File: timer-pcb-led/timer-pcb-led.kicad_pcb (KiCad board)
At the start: 4 copper layers, 74.5 x 54 mm, 15 parts, among them J1 JST_03

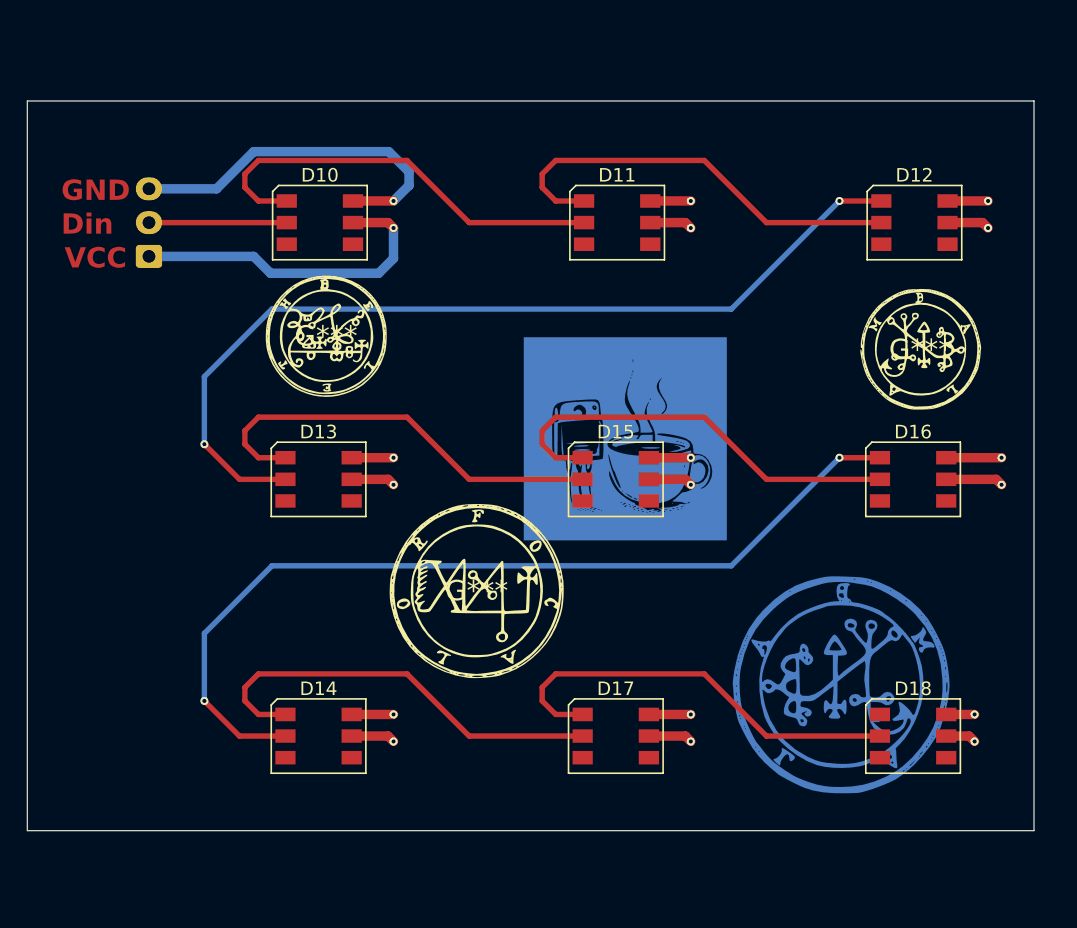
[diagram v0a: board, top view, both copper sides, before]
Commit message: rework des PCB stepper et led. création du PCB chargeur
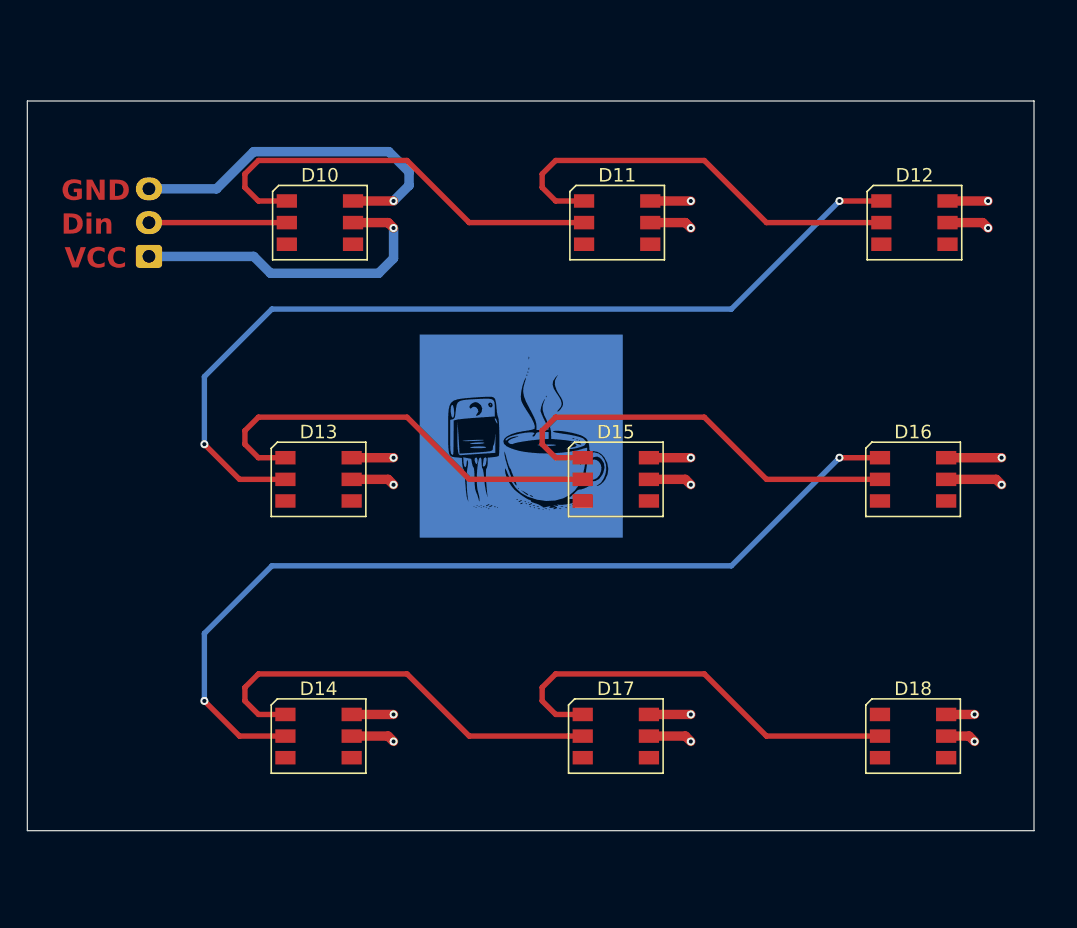
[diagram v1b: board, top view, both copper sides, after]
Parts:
- removed the G*** at (73.1, 136.4)
- removed the G*** at (84.2, 155.2)
- removed the G*** at (117.1, 137.4)
- removed the G*** at (111.2, 162.2)
- moved G*** 7.70 mm to (87.5, 143.8)

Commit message: suppression du dossier chargeur. integration de la partie chargeur usb-c sur le PCB stepper
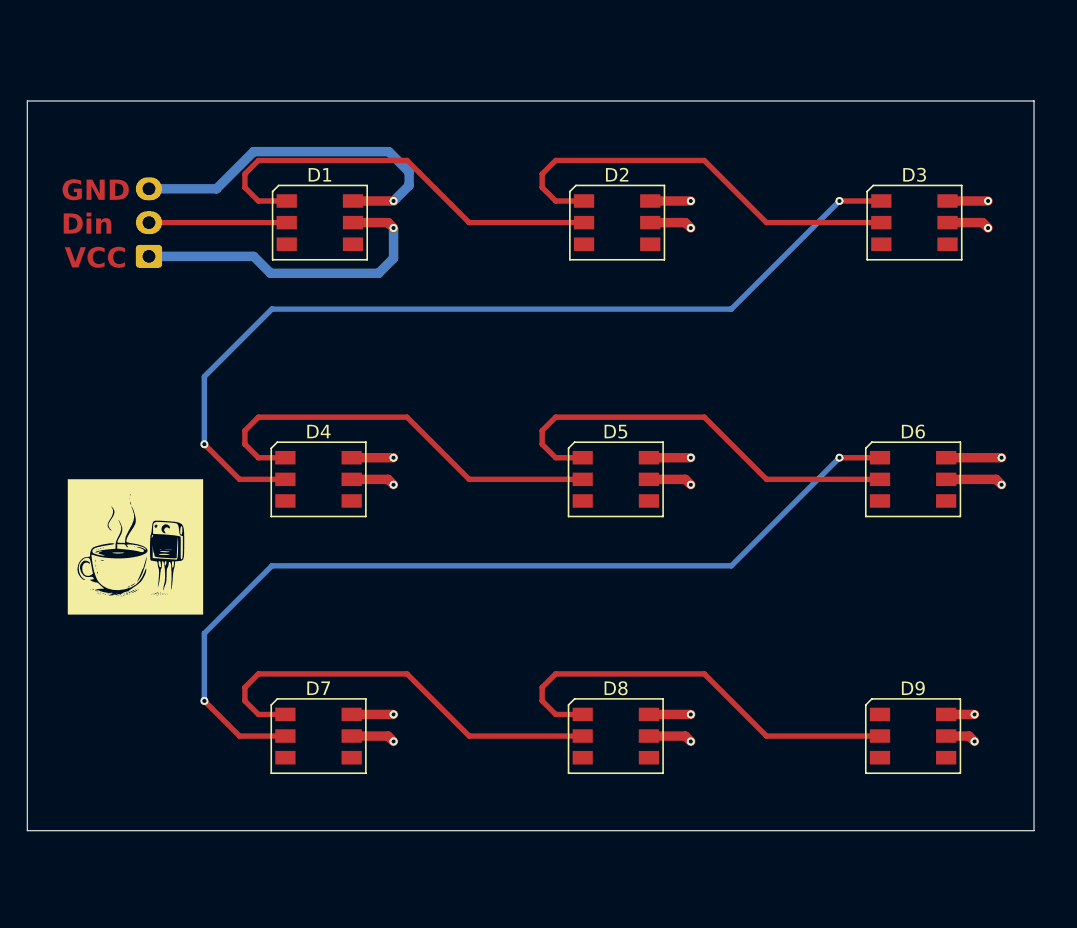
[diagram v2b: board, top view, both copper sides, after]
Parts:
- removed the G*** at (87.5, 143.8)
- added G***: LOGO, image.preety:logo_electrocafe_10x10, F.Cu at (59.0, 152.0)
- renumbered D10 to D1, D11 to D2, D12 to D3, D13 to D4, D15 to D5, D16 to D6, D14 to D7, D17 to D8, D18 to D9

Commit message: reroutage des liaisons pour avoir un circuit imprimé plus propre.
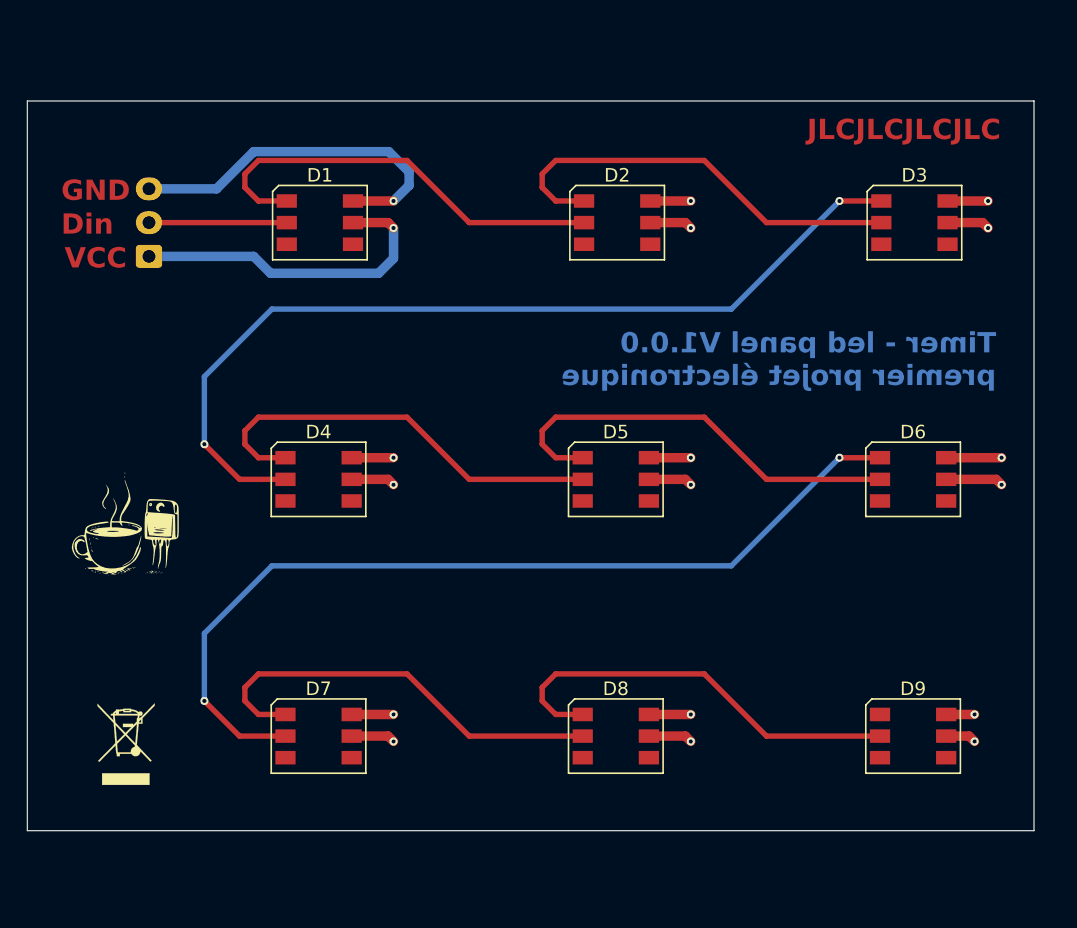
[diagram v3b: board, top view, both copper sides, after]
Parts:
- added REF**: WEEE-Logo_4.2x6mm_SilkScreen, Symbol:WEEE-Logo_4.2x6mm_SilkScreen, F.Cu at (58.3, 166.6)
- moved G*** 1.65 mm to (58.6, 150.4)
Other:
- board text added: "JLCJLCJLCJLC"
- board text added: "Timer - led panel V1.0.0 premier projet électronique"

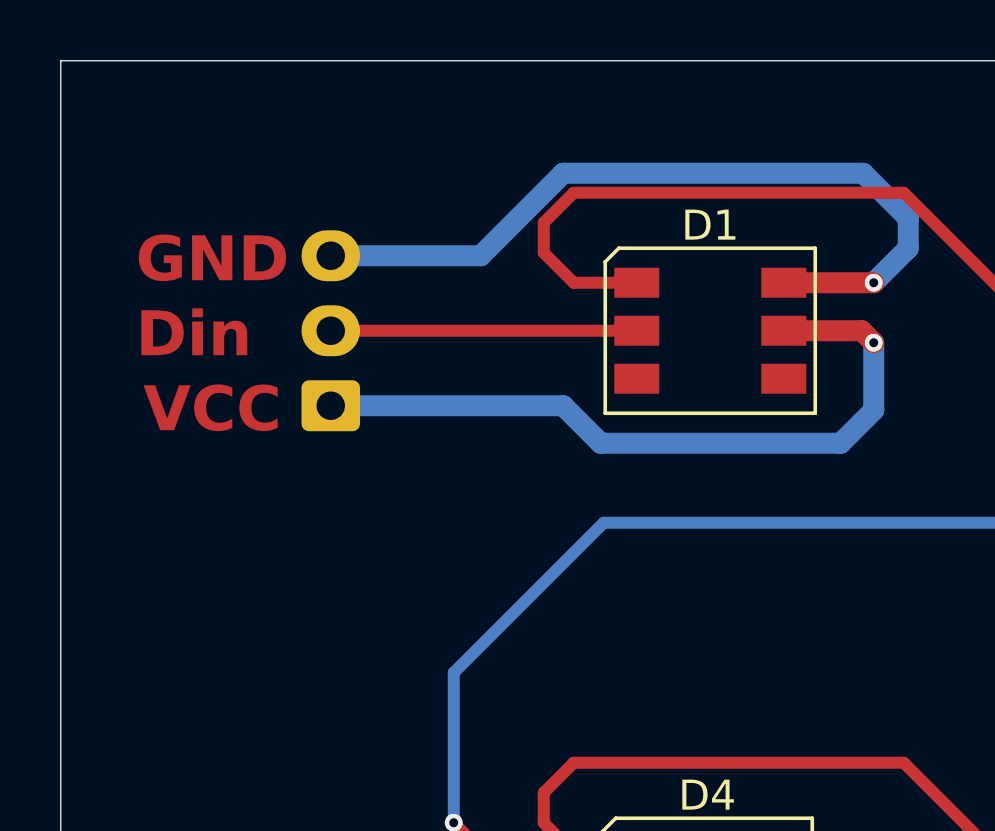
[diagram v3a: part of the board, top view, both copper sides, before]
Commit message: ajout de text indicatif couche silkscreen sur les différents composants du PCB. ajout de test points sur 5V, GND, GPIO37 pour debugger et pin 15 (3.3V). connecteurs repositionés franc bord.
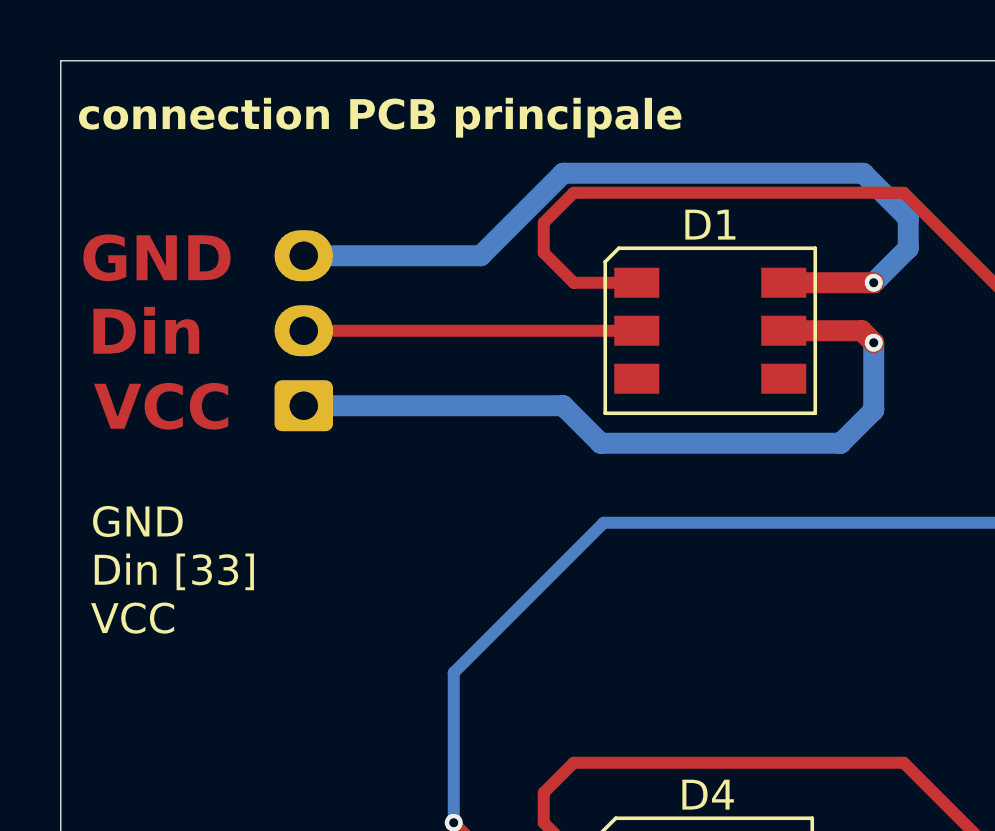
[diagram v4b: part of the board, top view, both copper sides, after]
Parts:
- moved J1 0.90 mm to (59.1, 130.5)
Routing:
- net +5V: track 50.4 -> 51.3 mm
- net GPIO33: track 10.2 -> 11.1 mm
- net GND: track 51.2 -> 52.1 mm
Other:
- board text added: "GND Din [33] VCC"
- board text added: "connection PCB principale"
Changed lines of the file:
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@@
 	(footprint "Connector_JST:JST_XH_S3B-XH-A-1_1x03_P2.50mm_Horizontal"
 		(layer "B.Cu")
-		(at 60 130.5 90)
+		(at 59.1 130.5 90)
 		(descr "JST XH series connector, S3B-XH-A-1 (http://www.jst-mfg.com/product/pdf/eng/eXH.pdf), generated with kicad-footprint-generator")
 		(tags "connector JST XH horizontal")
@@
 	)
 	(gr_text "GND"
-		(at 53.5 126.5 0)
+		(at 51.65 126.5 0)
 		(layer "F.Cu")
 		(effects
@@
 	)
 	(gr_text "Din"
-		(at 53.5 129 0)
+		(at 51.9 128.95 0)
 		(layer "F.Cu")
 		(effects
@@
 	)
 	(gr_text "VCC"
-		(at 53.75 131.5 0)
+		(at 52.1 131.45 0)
 		(layer "F.Cu")
 		(effects
@@
 		)
 	)
+	(gr_text "connection PCB principale"
+		(at 51.55 121.4 0)
+		(layer "F.SilkS")
+		(effects
+			(font
+				(size 1 1)
+				(thickness 0.25)
+				(bold yes)
+			)
+			(justify left bottom)
+		)
+	)
+	(gr_text "GND\nDin [33]\nVCC"
+		(at 52 138.2 0)
+		(layer "F.SilkS")
+		(effects
+			(font
+				(size 1 1)
+				(thickness 0.125)
+			)
+			(justify left bottom)
+		)
+	)
 	(segment
 		(start 97 145.4)
@@
 	)
 	(segment
-		(start 65 125.5)
-		(end 60 125.5)
+		(start 67.75 122.75)
+		(end 65 125.5)
+		(width 0.7)
+		(layer "B.Cu")
+		(net 1)
+	)
+	(segment
+		(start 79.25 125.25)
+		(end 79.25 124.25)
+		(width 0.7)
+		(layer "B.Cu")
+		(net 1)
+	)
+	(segment
+		(start 77.75 122.75)
+		(end 67.75 122.75)
 		(width 0.7)
 		(layer "B.Cu")
@@
 	)
 	(segment
-		(start 67.75 122.75)
-		(end 65 125.5)
-		(width 0.7)
-		(layer "B.Cu")
-		(net 1)
-	)
-	(segment
-		(start 77.75 122.75)
-		(end 67.75 122.75)
-		(width 0.7)
-		(layer "B.Cu")
-		(net 1)
-	)
-	(segment
-		(start 79.25 125.25)
-		(end 79.25 124.25)
+		(start 65 125.5)
+		(end 59.1 125.5)
 		(width 0.7)
 		(layer "B.Cu")
@@
 	(segment
 		(start 70.2 128)
-		(end 60 128)
+		(end 59.1 128)
 		(width 0.4)
 		(layer "F.Cu")
@@
 	)
 	(segment
+		(start 78.1 128.4)
+		(end 78.1 130.65)
+		(width 0.7)
+		(layer "B.Cu")
+		(net 9)
+	)
+	(segment
+		(start 77 131.75)
+		(end 69 131.75)
+		(width 0.7)
+		(layer "B.Cu")
+		(net 9)
+	)
+	(segment
+		(start 67.75 130.5)
+		(end 59.1 130.5)
+		(width 0.7)
+		(layer "B.Cu")
+		(net 9)
+	)
+	(segment
+		(start 78.1 130.65)
+		(end 77 131.75)
+		(width 0.7)
+		(layer "B.Cu")
+		(net 9)
+	)
+	(segment
 		(start 69 131.75)
 		(end 67.75 130.5)
 		(width 0.7)
 		(layer "B.Cu")
-		(net 9)
-	)
-	(segment
-		(start 77 131.75)
-		(end 69 131.75)
-		(width 0.7)
-		(layer "B.Cu")
-		(net 9)
-	)
-	(segment
-		(start 78.1 128.4)
-		(end 78.1 130.65)
-		(width 0.7)
-		(layer "B.Cu")
-		(net 9)
-	)
-	(segment
-		(start 78.1 130.65)
-		(end 77 131.75)
-		(width 0.7)
-		(layer "B.Cu")
-		(net 9)
-	)
-	(segment
-		(start 67.75 130.5)
-		(end 60 130.5)
-		(width 0.7)
-		(layer "B.Cu")

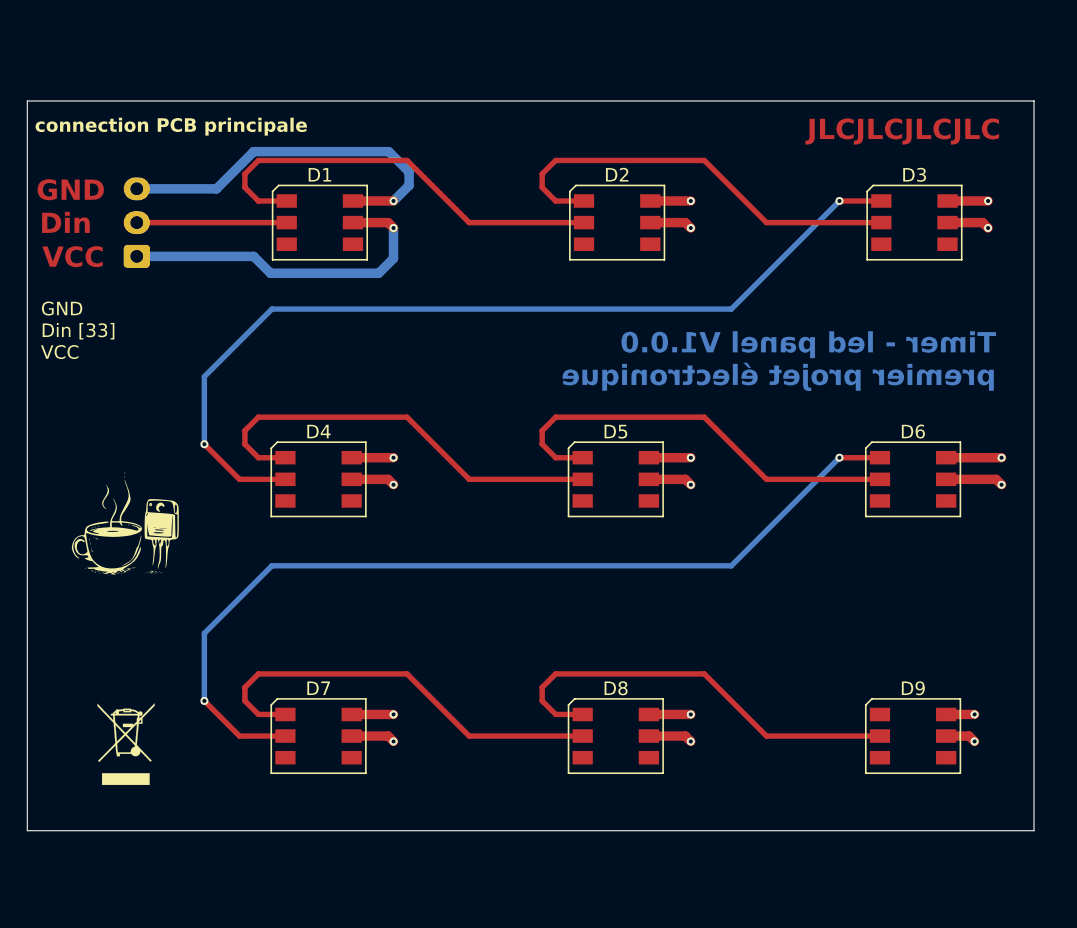
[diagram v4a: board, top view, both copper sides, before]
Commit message: mise à jour fichier blender pour impression 3D. Reste a mettre la bonne épaisseur pour le socle de la shell et percer les trous pour interrupteurs switch et on-off. déterminer ou placer entrées pour recharge et update code. comment fixer module recharge.
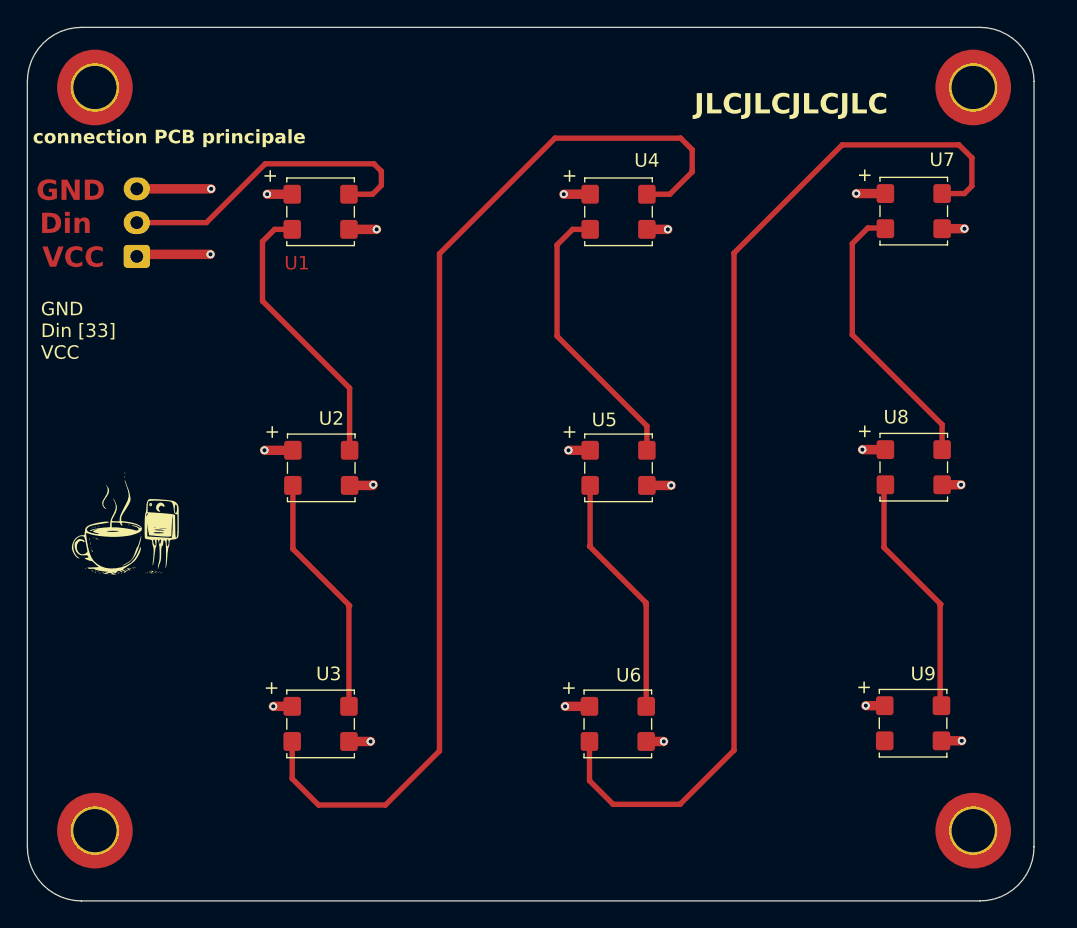
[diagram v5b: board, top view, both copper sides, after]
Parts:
- removed D1, D2, D3, D4, D5, D6, D7, D8, D9: WS2812, LED_SMD:LED_WS2812_PLCC6_5.0x5.0mm_P1.6mm
- removed REF**: WEEE-Logo_4.2x6mm_SilkScreen, Symbol:WEEE-Logo_4.2x6mm_SilkScreen
- added H1: MountingHole, MountingHole:MountingHole_3.2mm_M3_DIN965_Pad_TopOnly, F.Cu at (121.0, 118.0)
- added H2: MountingHole, MountingHole:MountingHole_3.2mm_M3_DIN965_Pad_TopOnly, F.Cu at (56.0, 118.0)
- added H3: MountingHole, MountingHole:MountingHole_3.2mm_M3_DIN965_Pad_TopOnly, F.Cu at (121.0, 173.0)
- added H4: MountingHole, MountingHole:MountingHole_3.2mm_M3_DIN965_Pad_TopOnly, F.Cu at (56.0, 173.0)
- added U1: , 1_My_Custom_Library:WS2812B-Xinlight-5050RGBC, F.Cu at (70.2, 124.7)
- added U2: ~, 1_My_Custom_Library:WS2812B-Xinlight-5050RGBC, F.Cu at (70.2, 143.7)
- added U3: ~, 1_My_Custom_Library:WS2812B-Xinlight-5050RGBC, F.Cu at (70.2, 162.6)
- added U4: ~, 1_My_Custom_Library:WS2812B-Xinlight-5050RGBC, F.Cu at (92.2, 124.7)
- added U5: ~, 1_My_Custom_Library:WS2812B-Xinlight-5050RGBC, F.Cu at (92.2, 143.7)
- added U6: ~, 1_My_Custom_Library:WS2812B-Xinlight-5050RGBC, F.Cu at (92.2, 162.6)
- added U7: ~, 1_My_Custom_Library:WS2812B-Xinlight-5050RGBC, F.Cu at (114.1, 124.7)
- added U8: ~, 1_My_Custom_Library:WS2812B-Xinlight-5050RGBC, F.Cu at (114.1, 143.6)
- added U9: ~, 1_My_Custom_Library:WS2812B-Xinlight-5050RGBC, F.Cu at (114.0, 162.6)
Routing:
- net Net-(U3-Dout): track 0.00 -> 81.2 mm
- net Net-(U6-Dout): track 0.00 -> 78.5 mm
- net Net-(D3-DOUT): track 67.6 -> 0.00 mm, vias 2 -> 0
- net Net-(D6-DOUT): track 67.5 -> 0.00 mm, vias 2 -> 0
- net GND: track 52.1 -> 20.1 mm, vias 9 -> 10
- net Net-(D2-DOUT): track 31.9 -> 0.00 mm
- net Net-(D1-DOUT): track 31.9 -> 0.00 mm
- net Net-(D8-DOUT): track 31.7 -> 0.00 mm
- net Net-(D7-DOUT): track 31.7 -> 0.00 mm
- net Net-(D5-DOUT): track 31.7 -> 0.00 mm
- net Net-(D4-DOUT): track 31.7 -> 0.00 mm
- net +5V: track 51.3 -> 21.5 mm, vias 9 -> 10
- net Net-(U7-Dout): track 0.00 -> 20.9 mm
- net Net-(U4-Dout): track 0.00 -> 20.9 mm
- net Net-(U1-Dout): track 0.00 -> 20.7 mm
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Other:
- board size 74.5 x 54 mm -> 74.5 x 64.6 mm
